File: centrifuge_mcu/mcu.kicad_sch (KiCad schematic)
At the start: 19 parts, among them J109 Conn_02x10_Odd_Even, J110 Conn_02x07_Counter_Clockwise, U105 EFM32GG990F1024, Y101 VXM7-1366-48M0000000

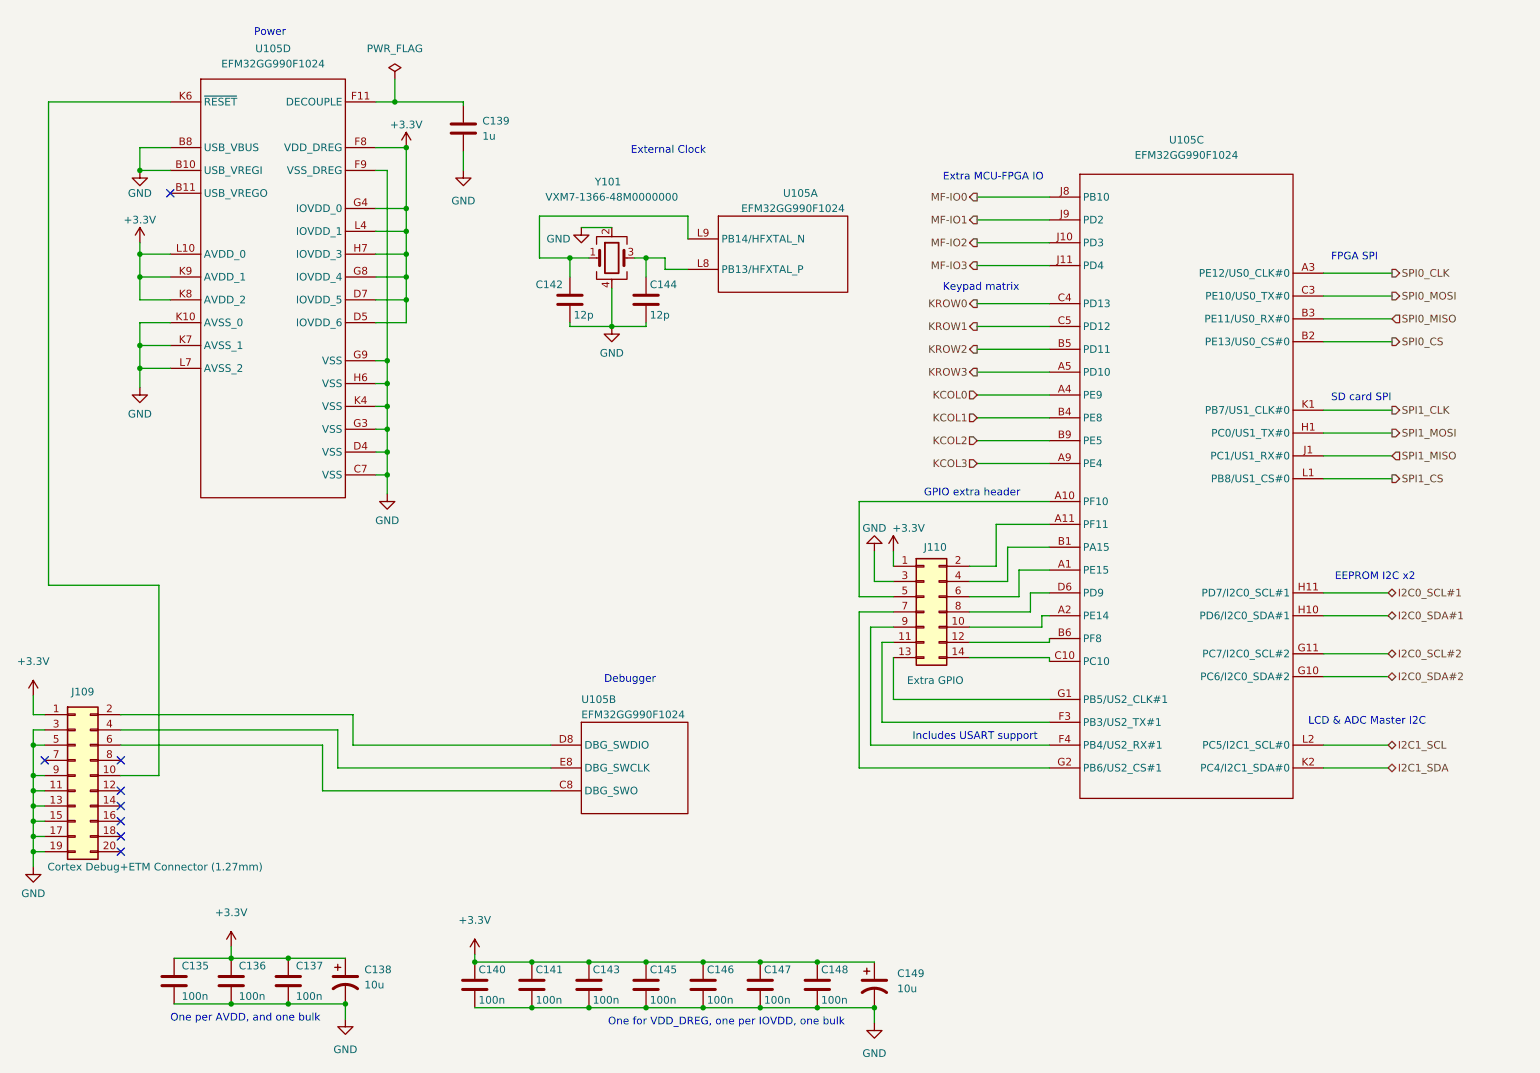
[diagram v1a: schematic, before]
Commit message: more footprints, add links to resistor and inductance purchase
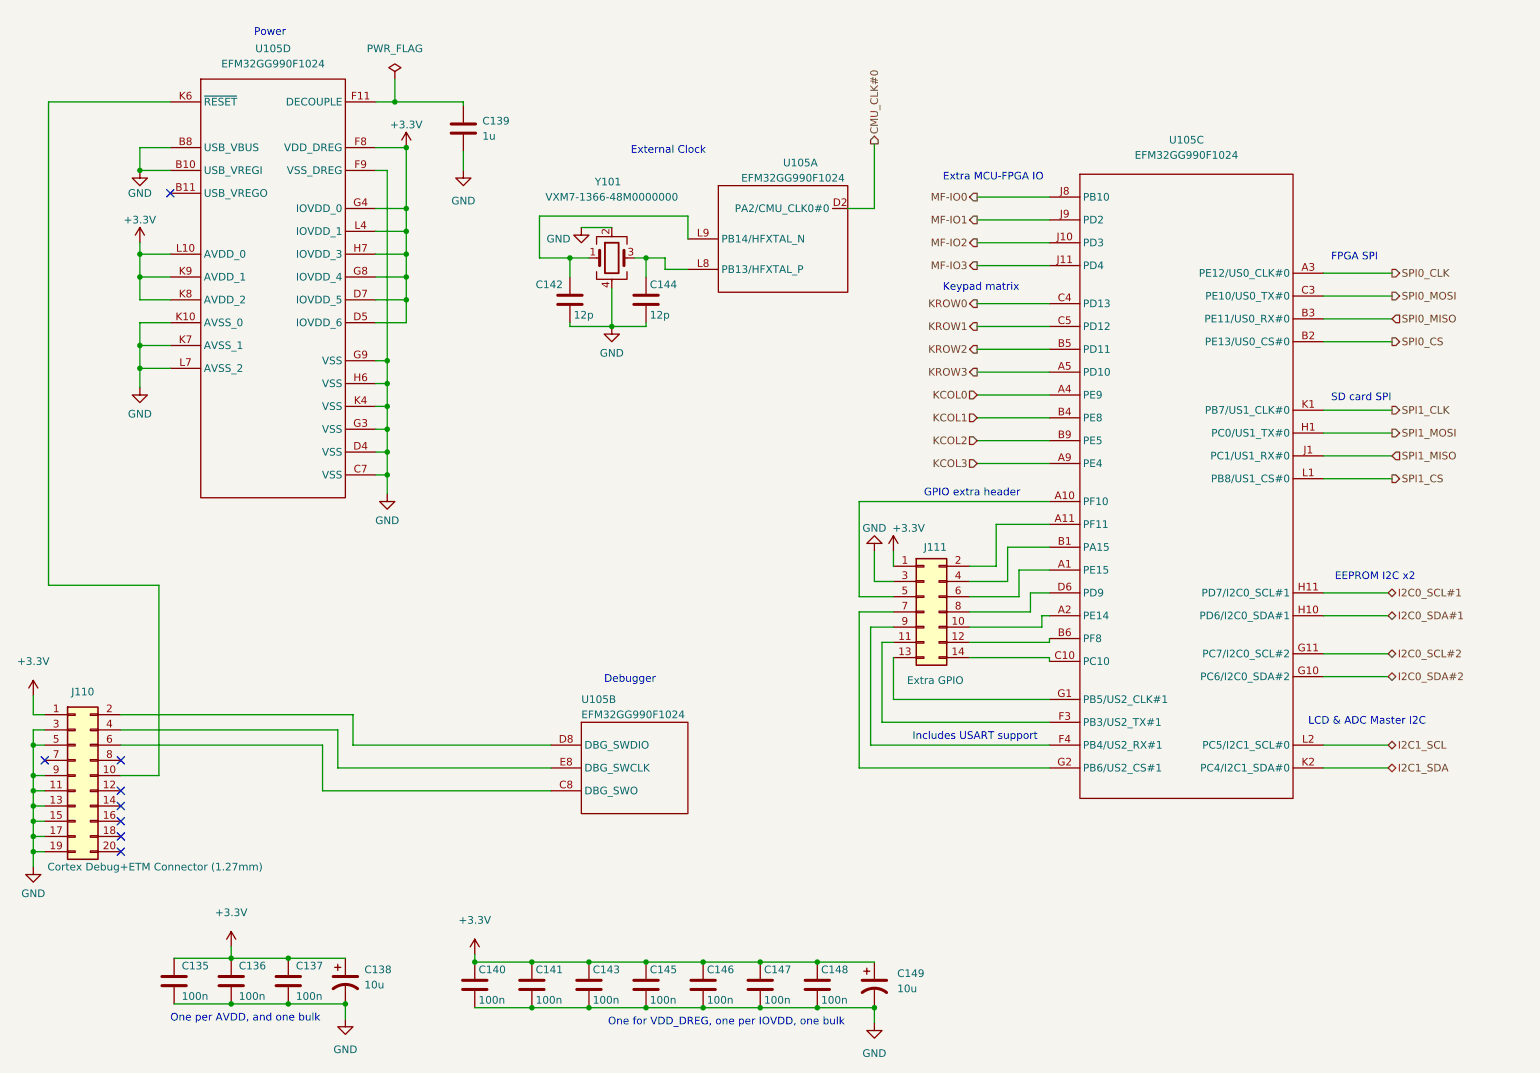
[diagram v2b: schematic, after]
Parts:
- renumbered J109 to J110, J110 to J111
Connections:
- new net CMU_CLK#0: U105.D2 (PA2/CMU_CLK0#0)
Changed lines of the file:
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@@
+    (stroke (width 0) (type default) (color 0 0 0 0))
+  )
+  (wire (pts (xy 163.195 50.8) (xy 163.195 40.005))
     (stroke (width 0) (type default) (color 0 0 0 0))
   )
@@
   )
   (wire (pts (xy 179.07 123.19) (xy 192.405 123.19))
+    (stroke (width 0) (type default) (color 0 0 0 0))
+  )
+  (wire (pts (xy 158.75 50.8) (xy 163.195 50.8))
     (stroke (width 0) (type default) (color 0 0 0 0))
   )
@@
     (effects (font (size 1.27 1.27)) (justify left))
   )
+  (hierarchical_label "CMU_CLK#0" (shape output) (at 163.195 40.005 90)
+    (effects (font (size 1.27 1.27)) (justify left))
+  )
   (hierarchical_label "KCOL2" (shape input) (at 180.34 89.535 180)
     (effects (font (size 1.27 1.27)) (justify right))
@@
       (effects (font (size 1.27 1.27)) hide)
     )
+    (pin "D2")
     (pin "L8")
     (pin "L9")
@@
   (symbol (lib_id "power:GND") (at 22.86 160.655 0) (unit 1)
     (in_bom yes) (on_board yes) (fields_autoplaced)
-    (property "Reference" "#PWR0124" (id 0) (at 22.86 167.005 0)
+    (property "Reference" "#PWR0121" (id 0) (at 22.86 167.005 0)
       (effects (font (size 1.27 1.27)) hide)
     )
@@
   (symbol (lib_id "power:GND") (at 163.195 186.69 0) (unit 1)
     (in_bom yes) (on_board yes) (fields_autoplaced)
-    (property "Reference" "#PWR0137" (id 0) (at 163.195 193.04 0)
+    (property "Reference" "#PWR0134" (id 0) (at 163.195 193.04 0)
       (effects (font (size 1.27 1.27)) hide)
     )
@@
   (symbol (lib_id "power:+3.3V") (at 40.64 56.515 0) (unit 1)
     (in_bom yes) (on_board yes)
-    (property "Reference" "#PWR0126" (id 0) (at 40.64 60.325 0)
+    (property "Reference" "#PWR0123" (id 0) (at 40.64 60.325 0)
       (effects (font (size 1.27 1.27)) hide)
     )
@@
   (symbol (lib_id "power:GND") (at 163.195 107.95 180) (unit 1)
     (in_bom yes) (on_board yes)
-    (property "Reference" "#PWR0136" (id 0) (at 163.195 101.6 0)
+    (property "Reference" "#PWR0133" (id 0) (at 163.195 101.6 0)
       (effects (font (size 1.27 1.27)) hide)
     )
@@
   (symbol (lib_id "power:+3.3V") (at 166.37 107.95 0) (unit 1)
     (in_bom yes) (on_board yes)
-    (property "Reference" "#PWR0138" (id 0) (at 166.37 111.76 0)
+    (property "Reference" "#PWR0135" (id 0) (at 166.37 111.76 0)
       (effects (font (size 1.27 1.27)) hide)
     )
@@
   (symbol (lib_id "power:GND") (at 40.64 80.645 0) (unit 1)
     (in_bom yes) (on_board yes) (fields_autoplaced)
-    (property "Reference" "#PWR0127" (id 0) (at 40.64 86.995 0)
+    (property "Reference" "#PWR0124" (id 0) (at 40.64 86.995 0)
       (effects (font (size 1.27 1.27)) hide)
     )
@@
   (symbol (lib_id "power:+3.3V") (at 22.86 132.08 0) (unit 1)
     (in_bom yes) (on_board yes) (fields_autoplaced)
-    (property "Reference" "#PWR0123" (id 0) (at 22.86 135.89 0)
+    (property "Reference" "#PWR0120" (id 0) (at 22.86 135.89 0)
       (effects (font (size 1.27 1.27)) hide)
     )
@@
   (symbol (lib_id "Connector_Generic:Conn_02x10_Odd_Even") (at 29.845 145.415 0) (unit 1)
     (in_bom yes) (on_board yes)
-    (property "Reference" "J109" (id 0) (at 31.115 131.445 0))
+    (property "Reference" "J110" (id 0) (at 31.115 131.445 0))
     (property "Value" "Conn_02x10_Odd_Even" (id 1) (at 31.115 130.81 0)
       (effects (font (size 1.27 1.27)) hide)
@@
   (symbol (lib_id "power:GND") (at 74.93 186.055 0) (unit 1)
     (in_bom yes) (on_board yes) (fields_autoplaced)
-    (property "Reference" "#PWR0129" (id 0) (at 74.93 192.405 0)
+    (property "Reference" "#PWR0126" (id 0) (at 74.93 192.405 0)
       (effects (font (size 1.27 1.27)) hide)
     )
@@
   (symbol (lib_id "power:GND") (at 94.615 44.45 0) (unit 1)
     (in_bom yes) (on_board yes) (fields_autoplaced)
-    (property "Reference" "#PWR0132" (id 0) (at 94.615 50.8 0)
+    (property "Reference" "#PWR0129" (id 0) (at 94.615 50.8 0)
       (effects (font (size 1.27 1.27)) hide)
     )
@@
   (symbol (lib_id "power:PWR_FLAG") (at 83.185 29.21 0) (unit 1)
     (in_bom yes) (on_board yes) (fields_autoplaced)
-    (property "Reference" "#FLG0107" (id 0) (at 83.185 27.305 0)
+    (property "Reference" "#FLG0108" (id 0) (at 83.185 27.305 0)
       (effects (font (size 1.27 1.27)) hide)
     )
@@
   (symbol (lib_id "power:GND") (at 40.64 44.45 0) (unit 1)
     (in_bom yes) (on_board yes)
-    (property "Reference" "#PWR0125" (id 0) (at 40.64 50.8 0)
+    (property "Reference" "#PWR0122" (id 0) (at 40.64 50.8 0)
       (effects (font (size 1.27 1.27)) hide)
     )
@@
   (symbol (lib_id "power:+3.3V") (at 85.09 40.64 0) (unit 1)
     (in_bom yes) (on_board yes)
-    (property "Reference" "#PWR0131" (id 0) (at 85.09 44.45 0)
+    (property "Reference" "#PWR0128" (id 0) (at 85.09 44.45 0)
       (effects (font (size 1.27 1.27)) hide)
     )
@@
   (symbol (lib_id "power:+3.3V") (at 55.88 173.99 0) (unit 1)
     (in_bom yes) (on_board yes) (fields_autoplaced)
-    (property "Reference" "#PWR0128" (id 0) (at 55.88 177.8 0)
+    (property "Reference" "#PWR0125" (id 0) (at 55.88 177.8 0)
       (effects (font (size 1.27 1.27)) hide)
     )
@@
     (pin "2")
   )
-  (symbol (lib_id "mcu_centrifuge_library:EFM32GG990F1024") (at 148.59 55.88 0) (unit 1)
-    (in_bom yes) (on_board yes)
-    (property "Reference" "U105" (id 0) (at 147.955 48.26 0)
-      (effects (font (size 1.27 1.27)) (justify left))
-    )
-    (property "Value" "EFM32GG990F1024" (id 1) (at 140.97 50.8 0)
+  (symbol (lib_name "EFM32GG990F1024_1") (lib_id "mcu_centrifuge_library:EFM32GG990F1024") (at 148.59 55.88 0) (unit 1)
+    (in_bom yes) (on_board yes)
+    (property "Reference" "U105" (id 0) (at 147.955 43.18 0)
+      (effects (font (size 1.27 1.27)) (justify left))
+    )
+    (property "Value" "EFM32GG990F1024" (id 1) (at 140.97 45.72 0)
       (effects (font (size 1.27 1.27)) (justify left))
     )
@@
       (effects (font (size 1.27 1.27)) hide)
     )
+    (pin "D2")
     (pin "L8")
     (pin "L9")
@@
   (symbol (lib_id "power:GND") (at 119.38 70.485 0) (unit 1)
     (in_bom yes) (on_board yes) (fields_autoplaced)
-    (property "Reference" "#PWR0135" (id 0) (at 119.38 76.835 0)
+    (property "Reference" "#PWR0132" (id 0) (at 119.38 76.835 0)
       (effects (font (size 1.27 1.27)) hide)
     )
@@
   (symbol (lib_id "Connector_Generic:Conn_02x07_Odd_Even") (at 171.45 118.11 0) (unit 1)
     (in_bom yes) (on_board yes)
-    (property "Reference" "J110" (id 0) (at 173.355 107.315 0))
+    (property "Reference" "J111" (id 0) (at 173.355 107.315 0))
     (property "Value" "Conn_02x07_Counter_Clockwise" (id 1) (at 172.72 109.22 0)
       (effects (font (size 1.27 1.27)) hide)
@@
   (symbol (lib_id "power:GND") (at 81.915 98.425 0) (unit 1)
     (in_bom yes) (on_board yes) (fields_autoplaced)
-    (property "Reference" "#PWR0130" (id 0) (at 81.915 104.775 0)
+    (property "Reference" "#PWR0127" (id 0) (at 81.915 104.775 0)
       (effects (font (size 1.27 1.27)) hide)
     )
@@
       (effects (font (size 1.27 1.27)) hide)
     )
+    (pin "D2")
     (pin "L8")
     (pin "L9")
@@
   (symbol (lib_id "power:+3.3V") (at 96.52 175.26 0) (unit 1)
     (in_bom yes) (on_board yes) (fields_autoplaced)
-    (property "Reference" "#PWR0133" (id 0) (at 96.52 179.07 0)
+    (property "Reference" "#PWR0130" (id 0) (at 96.52 179.07 0)
       (effects (font (size 1.27 1.27)) hide)
     )
@@
     (pin "1")
   )
-  (symbol (lib_name "EFM32GG990F1024_3") (lib_id "mcu_centrifuge_library:EFM32GG990F1024") (at 215.265 97.155 0) (unit 3)
+  (symbol (lib_id "mcu_centrifuge_library:EFM32GG990F1024") (at 215.265 97.155 0) (unit 3)
     (in_bom yes) (on_board yes) (fields_autoplaced)
     (property "Reference" "U105" (id 0) (at 215.265 39.37 0))
@@
       (effects (font (size 1.27 1.27)) hide)
     )
+    (pin "D2")
     (pin "L8")
     (pin "L9")
@@
   (symbol (lib_id "power:GND") (at 114.3 53.975 0) (unit 1)
     (in_bom yes) (on_board yes)
-    (property "Reference" "#PWR0134" (id 0) (at 114.3 60.325 0)
-      (effects (font (size 1.27 1.27)) hide)
-    )
+    (property "Reference" "#PWR0131" (id 0) (at 114.3 60.325 0)
+      (effects (font (size 1.27 1.27)) hide)
+    )

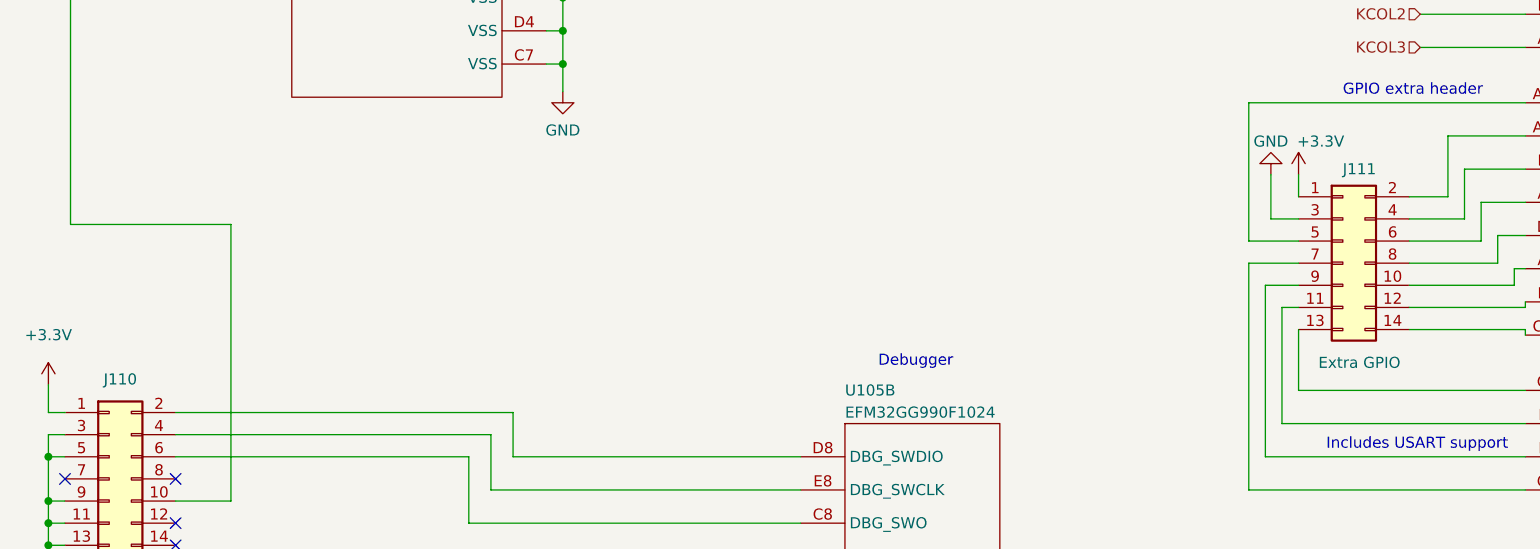
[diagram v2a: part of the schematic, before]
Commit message: last footprints, time to route (after final FPGA-board connectors)
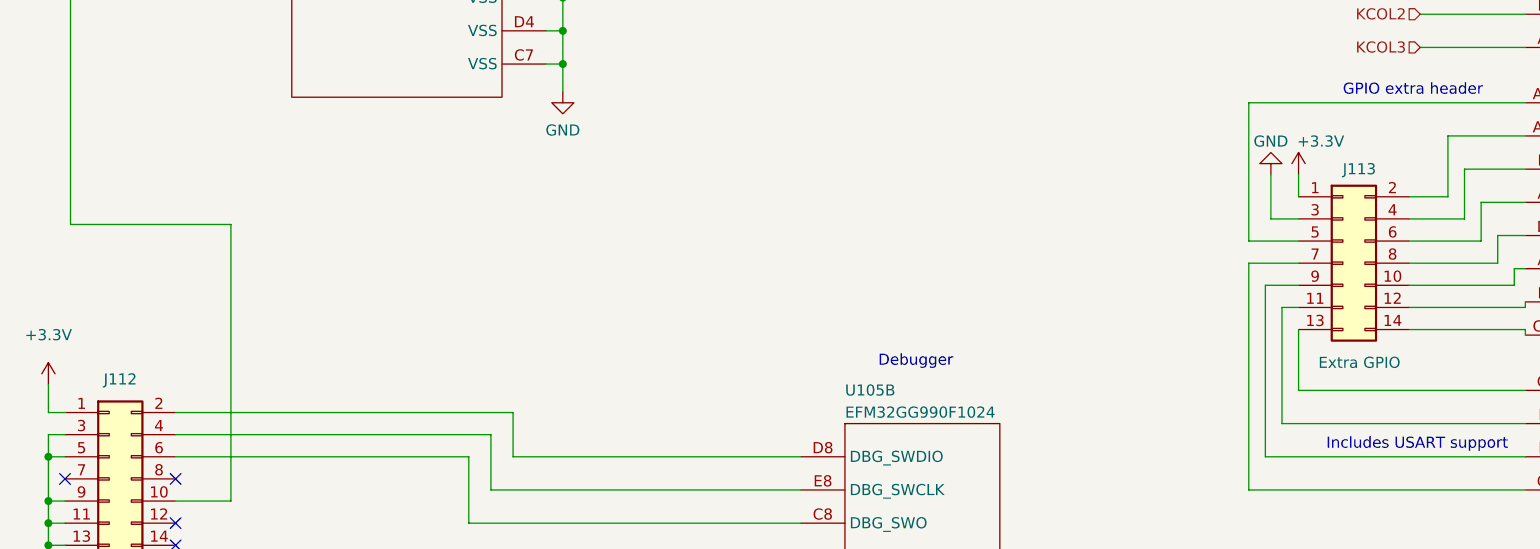
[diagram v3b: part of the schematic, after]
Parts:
- renumbered J110 to J112, J111 to J113
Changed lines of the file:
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@@
   (symbol (lib_id "Connector_Generic:Conn_02x10_Odd_Even") (at 29.845 145.415 0) (unit 1)
     (in_bom yes) (on_board yes)
-    (property "Reference" "J110" (id 0) (at 31.115 131.445 0))
+    (property "Reference" "J112" (id 0) (at 31.115 131.445 0))
     (property "Value" "Conn_02x10_Odd_Even" (id 1) (at 31.115 130.81 0)
       (effects (font (size 1.27 1.27)) hide)
@@
   (symbol (lib_id "Connector_Generic:Conn_02x07_Odd_Even") (at 171.45 118.11 0) (unit 1)
     (in_bom yes) (on_board yes)
-    (property "Reference" "J111" (id 0) (at 173.355 107.315 0))
+    (property "Reference" "J113" (id 0) (at 173.355 107.315 0))
     (property "Value" "Conn_02x07_Counter_Clockwise" (id 1) (at 172.72 109.22 0)
       (effects (font (size 1.27 1.27)) hide)

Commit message: start routing PCB for the MCU, starting with power
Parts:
- added D101: LED_YELLOW_2V_20mA, Diode_SMD:D_0805_2012Metric_Pad1.15x1.40mm_HandSolder, symbol Device:LED
- added Q102: Q_NMOS_GSD, Package_TO_SOT_SMD:SOT-323_SC-70_Handsoldering, symbol Device:Q_NMOS_GSD
- added R123: 62, Resistor_SMD:R_0805_2012Metric_Pad1.20x1.40mm_HandSolder, symbol Device:R
- J114: renamed from J113; value Conn_02x07_Counter_Clockwise -> Extra MCU GPIO; Title Extra GPIO -> (none)
- U106: renamed from U105; footprint (none) -> centrifuge_mcu:BGA-112_9.0x9.0mm_Layout11x11_P0.8mm_Ball0.4mm_Pad0.35mm_NSMD
- Y101: footprint Crystal:Crystal_SMD_TXC_7M-4Pin_3.2x2.5mm_HandSoldering -> centrifuge_mcu:Crystal_SMD_TXC_7M-4Pin_3.2x2.5mm_TIGHT
- renumbered J112 to J113
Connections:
- net +3.3V: now also R123.1
- net GND: now also Q102.2 (S)
- new net: Q102.1 (G), U106.C1 (PA1)
- new net: D101.1 (K), Q102.3 (D)
- new net: D101.2 (A), R123.2
- new net ADC0_RST: U106.L11 (PD0)
- new net ADC1_RST: U106.K11 (PD1)
- new net FPGA_CONFIG_DONE: U106.A8 (PF12)
- new net FPGA_INIT_B: U106.A6 (PF7)
- new net FPGA_PROGRAM_B: U106.A7 (PF5)
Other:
- note added: "ADC Reset"
- note added: "DDC I2C x2"
- note added: "FPGA control"
- note added: "Output blinky"
- note removed: "EEPROM I2C x2"

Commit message: connect everything in MCU pcb, connection time
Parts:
- C138, C149: footprint Capacitor_SMD:CP_Elec_4x5.4 -> Capacitor_SMD:C_0805_2012Metric_Pad1.18x1.45mm_HandSolder; symbol Device:C_Polarized_US -> Device:C; Purchase https://www.digikey.no/no/products/detail/nichicon/UWT1C100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 -> https://www.digikey.no/no/products/detail/yageo/CC0805MKX5R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
- J113: value Conn_02x10_Odd_Even -> DEBUG
- J114: footprint Connector_PinHeader_2.54mm:PinHeader_2x07_P2.54mm_Vertical -> Connector_PinHeader_2.54mm:PinHeader_2x04_P2.54mm_Vertical; symbol Connector_Generic:Conn_02x07_Odd_Even -> Connector_Generic:Conn_02x04_Odd_Even
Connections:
- net FPGA_CONFIG_DONE: now also U106.B1 (PA15); no longer U106.A8 (PF12)
- net FPGA_INIT_B: now also U106.C1 (PA1); no longer U106.A6 (PF7)
- net FPGA_PROGRAM_B: now also U106.C2 (PA0); no longer U106.A7 (PF5)
- net GND: now also J114.2 (Pin_2); no longer J114.3 (Pin_3)
- net KCOL0: now also U106.A11 (PF11); no longer U106.A4 (PE9)
- net KCOL1: now also U106.B9 (PE5); no longer U106.B4 (PE8)
- net KCOL2: now also U106.A10 (PF10); no longer U106.B9 (PE5)
- net KROW0: now also U106.A8 (PF12); no longer U106.C4 (PD13)
- net KROW1: now also U106.B7 (PF6); no longer U106.C5 (PD12)
- net KROW2: now also U106.A7 (PF5); no longer U106.B5 (PD11)
- net KROW3: now also U106.B6 (PF8); no longer U106.A5 (PD10)
- net MF-IO0: now also U106.A6 (PF7); no longer U106.J8 (PB10)
- net MF-IO1: now also U106.A5 (PD10); no longer U106.J9 (PD2)
- net MF-IO2: now also U106.A2 (PE14); no longer U106.J10 (PD3)
- net MF-IO3: now also U106.A1 (PE15); no longer U106.J11 (PD4)
- net at U106.G1 (PB5): now also J114.5 (Pin_5); no longer J114.13 (Pin_13)
- net at J114.4 (Pin_4): now also U106.D1 (PA3); no longer U106.B1 (PA15)
- net at J114.6 (Pin_6): now also U106.E1 (PA6); no longer U106.A1 (PE15)
- net at U106.G2 (PB6): now also J114.3 (Pin_3); no longer J114.7 (Pin_7)
- net at J114.8 (Pin_8): now also U106.E2 (PA5); no longer U106.D6 (PD9)
- net at Q102.1 (G): now also U106.L3 (PA14); no longer U106.C1 (PA1)
- new net: J114.7 (Pin_7), U106.F1 (PB1)
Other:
- note removed: "GPIO extra header"
- note removed: "Includes USART support"
